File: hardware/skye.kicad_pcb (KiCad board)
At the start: 2 copper layers, 13.2 x 24.5 mm, 12 parts, among them IC1 ATTINY85-20SUR, P1 IO, P2 IO, P3 USB_A, U1 WS2812

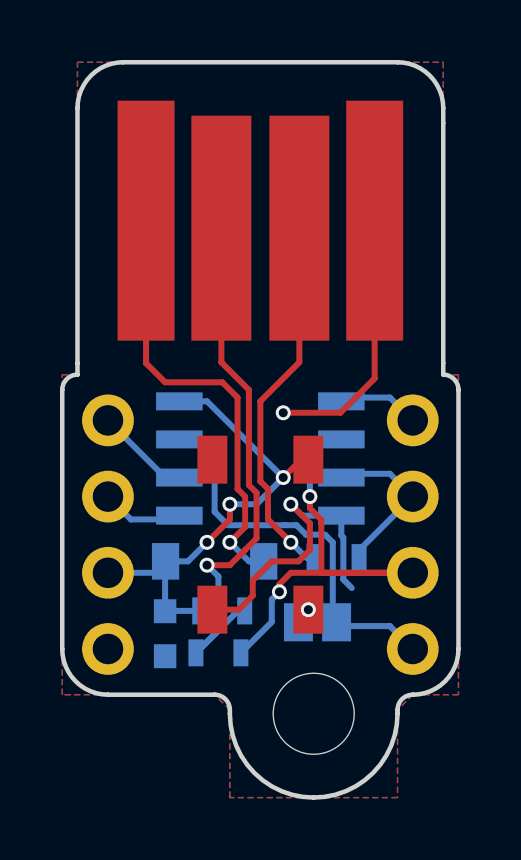
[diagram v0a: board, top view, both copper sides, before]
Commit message: Added zenier diodes
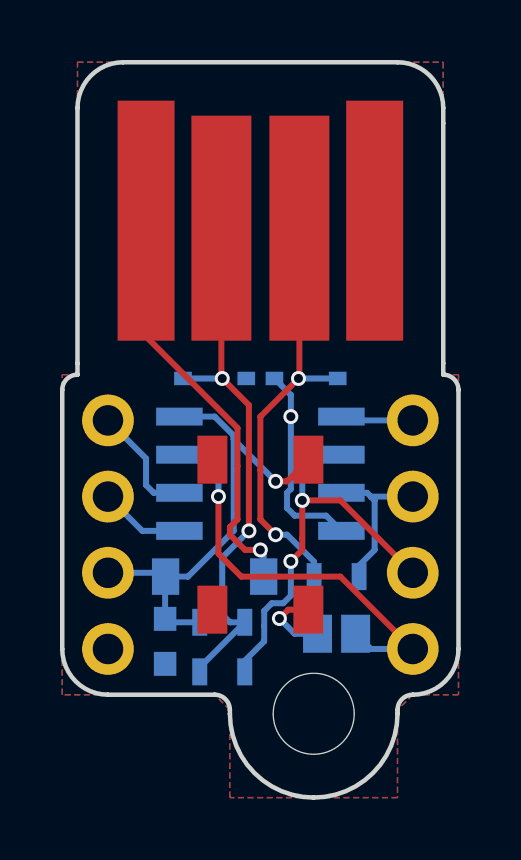
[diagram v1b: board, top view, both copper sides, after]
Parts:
- added D2: 3V6, Diodes_SMD:SOD-323, B.Cu at (159.8, 97.4)
- added D3: 3V6, Diodes_SMD:SOD-323, B.Cu at (162.8, 97.4)
- moved JP1 0.74 mm to (163.8, 105.9)
- moved R2 0.65 mm to (160.0, 107.2)
- moved R3 0.64 mm to (163.8, 104.0)
- moved D1 0.51 mm to (159.8, 104.0)
- moved IC1 0.51 mm to (161.3, 100.6)
- moved R1 0.38 mm to (160.0, 105.5)
- moved C1 0.25 mm to (158.1, 106.2)
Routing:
- net GND: track 19.2 -> 6.72 mm, vias 2 -> 1
- net Net-(IC1-Pad2): track 16.7 -> 13.9 mm
- net Net-(D3-Pad1): track 12.3 -> 14.5 mm, vias 1 -> 2
- net Net-(JP1-Pad2): track 0.56 -> 2.57 mm
- net Net-(IC1-Pad7): track 13.2 -> 14.4 mm, vias 0 -> 1
- net Net-(IC1-Pad6): track 3.17 -> 3.90 mm
- net Net-(D1-Pad2): track 14.7 -> 14.0 mm
- net +5V: track 15.9 -> 16.2 mm, vias 3 -> 1
- net Net-(D2-Pad1): track 18.3 -> 18.1 mm, vias 1 -> 2
